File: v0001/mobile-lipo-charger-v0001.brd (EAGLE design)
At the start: 82.9 x 96.2 mm, 82 parts, among them IC1 AD8610MR, IC3 AD8610MR, IC5 STM32F429NGH, SW2 DHT-4235A, T1 BC846, T2 BC846, T3 BC846, U3 3.3V, U4 3.3V

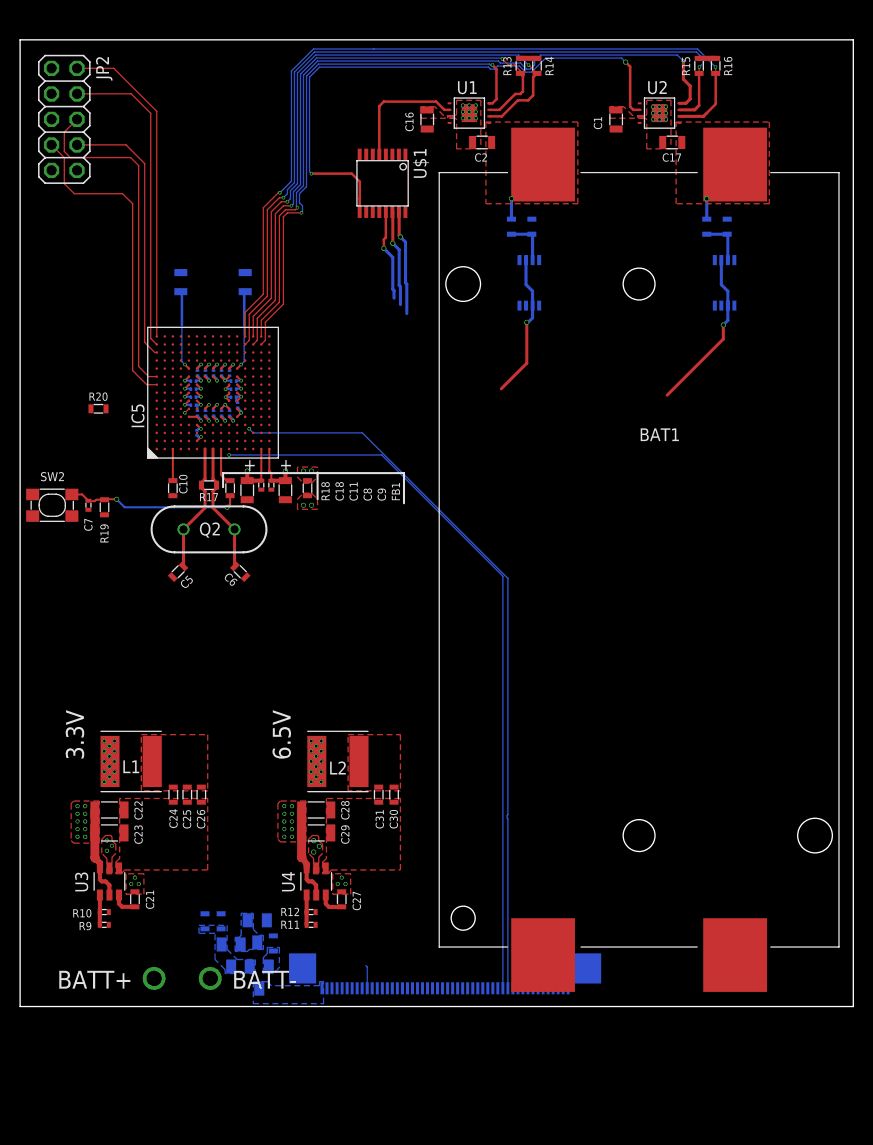
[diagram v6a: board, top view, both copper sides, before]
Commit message: TFT Routing
Began routing the TFT connections from the MCU BGA to the FPC
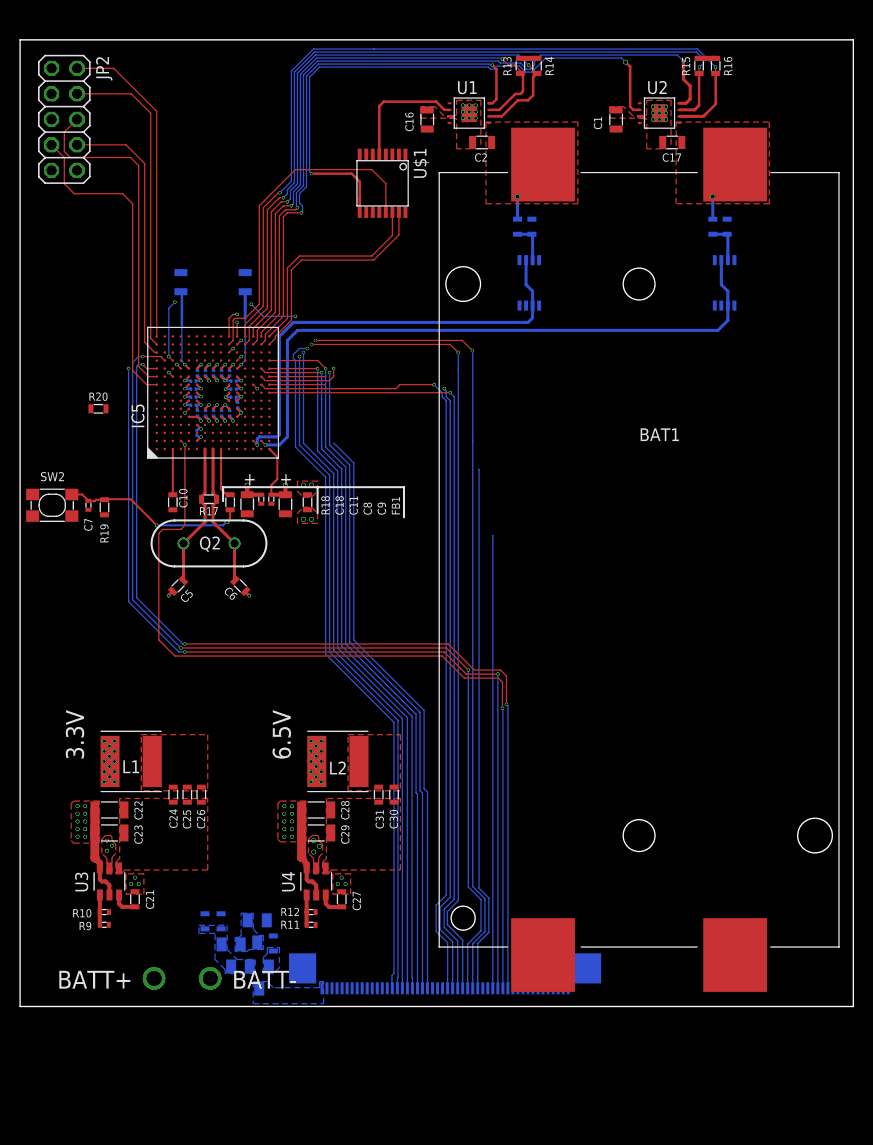
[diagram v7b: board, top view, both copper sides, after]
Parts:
- moved C10 1.40 mm to (15.2, 61.1)
- moved C11 1.40 mm to (24.0, 61.4)
- moved C18 1.40 mm to (22.6, 60.9)
- moved C5 1.40 mm to (15.7, 52.8)
- moved C6 1.40 mm to (21.9, 52.8)
- moved C8 1.40 mm to (25.0, 61.4)
- moved C9 1.40 mm to (26.4, 60.9)
- moved FB1 1.40 mm to (28.6, 61.1)
- moved Q2 1.40 mm to (18.8, 57.0)
- moved R17 1.40 mm to (18.8, 61.4)
- moved R18 1.40 mm to (20.9, 61.1)
- moved R7 0.60 mm to (68.9, 88.5)
- moved R5 0.60 mm to (49.5, 88.5)
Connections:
- removed net N$12: IC5.R15
- new net VREF+: IC5.P1
- net BATT1_V: now also IC5.N2
- net BATT2_V: now also IC5.P2
- net I_POT_SCLK: now also IC5.K14
- net I_POT_SDI: now also IC5.R15
- net I_POT_SDO: now also IC5.R14
- net VDDA: no longer IC5.P1
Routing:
- net DB3: track 0.00 -> 101.5 mm, vias 0 -> 6
- net LCD_WR: track 0.00 -> 98.9 mm, vias 0 -> 4
- net DB2: track 0.00 -> 96.3 mm, vias 0 -> 3
- net DB1: track 0.00 -> 95.0 mm, vias 0 -> 3
- net DB17: track 0.00 -> 80.5 mm, vias 0 -> 2
- net DB5: track 0.00 -> 80.0 mm, vias 0 -> 2
- net DB6: track 0.00 -> 79.0 mm, vias 0 -> 1
- net DB4: track 0.00 -> 78.4 mm, vias 0 -> 1
- net DB15: track 0.00 -> 77.1 mm, vias 0 -> 2
- net DB16: track 0.00 -> 76.4 mm, vias 0 -> 2
- net DB12: track 0.00 -> 71.4 mm, vias 0 -> 1
- net DB13: track 0.00 -> 71.2 mm, vias 0 -> 1
- net DB11: track 0.00 -> 70.7 mm, vias 0 -> 1
- net DB14: track 0.00 -> 70.2 mm, vias 0 -> 1
- net DB10: track 0.00 -> 66.5 mm, vias 0 -> 1
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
